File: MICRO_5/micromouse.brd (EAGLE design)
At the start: 96 x 72 mm, 34 parts

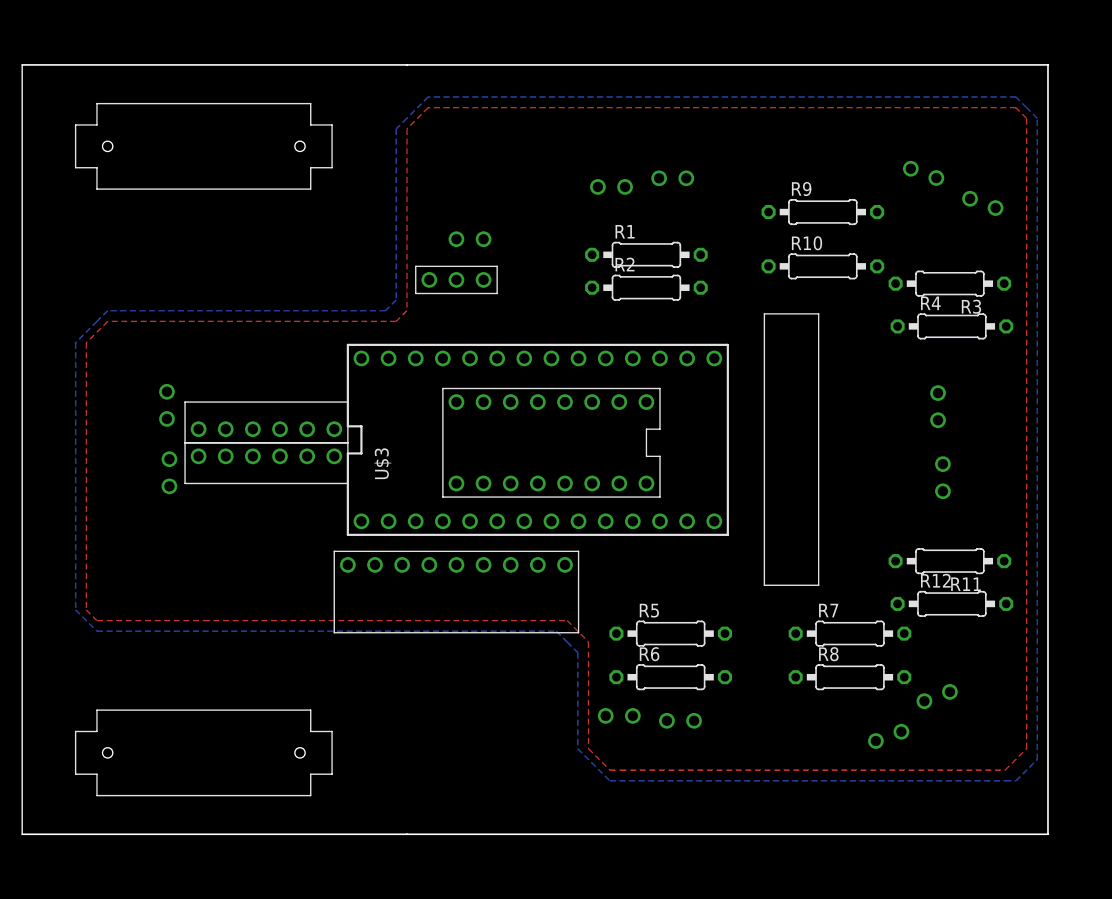
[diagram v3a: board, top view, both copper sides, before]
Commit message: put in led's into proper spacing so they fit onto the board. This is last commit before I start tracing so come back to this is somethings was wrong beforehand
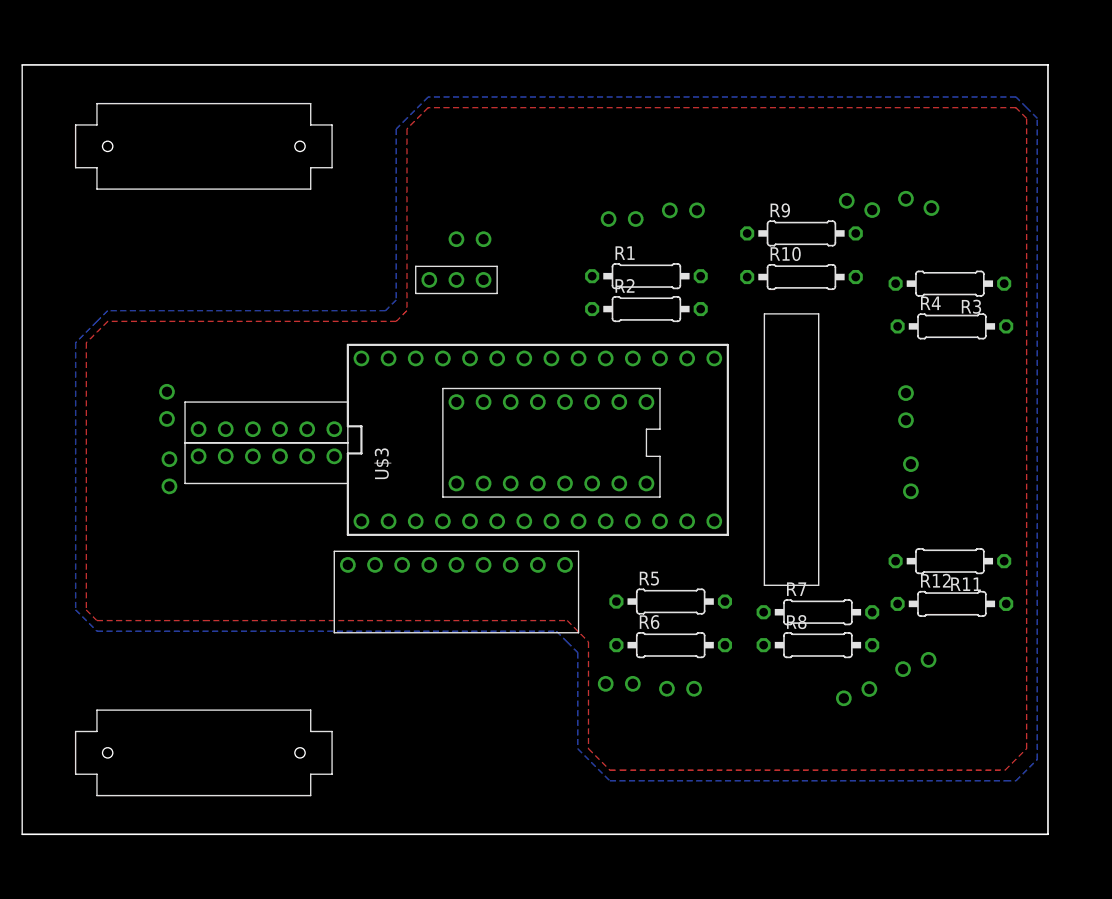
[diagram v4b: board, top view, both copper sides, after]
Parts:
- moved U$16 6.71 mm to (78.4, 62.9)
- moved U$17 6.00 mm to (83.9, 63.0)
- moved U$14 5.00 mm to (78.1, 17.2)
- moved R8 4.24 mm to (74.5, 21.7)
- moved R7 3.61 mm to (74.5, 24.8)
- moved U$15 3.61 mm to (83.6, 19.9)
- moved U$5 3.16 mm to (56.1, 61.6)
- moved U$9 3.16 mm to (61.9, 62.4)
- moved U$7 3.00 mm to (61.6, 17.6)
- moved R5 3.00 mm to (60.7, 25.8)
- moved R6 3.00 mm to (60.7, 21.7)
- moved U$12 3.00 mm to (82.7, 44.0)
- moved U$6 3.00 mm to (83.2, 37.4)
- moved U$8 3.00 mm to (55.9, 18.1)
- moved R9 2.83 mm to (72.9, 60.2)
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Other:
- outline, holes or cut-outs redrawn
